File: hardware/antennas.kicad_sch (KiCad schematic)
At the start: 21 parts, among them J1001 132134

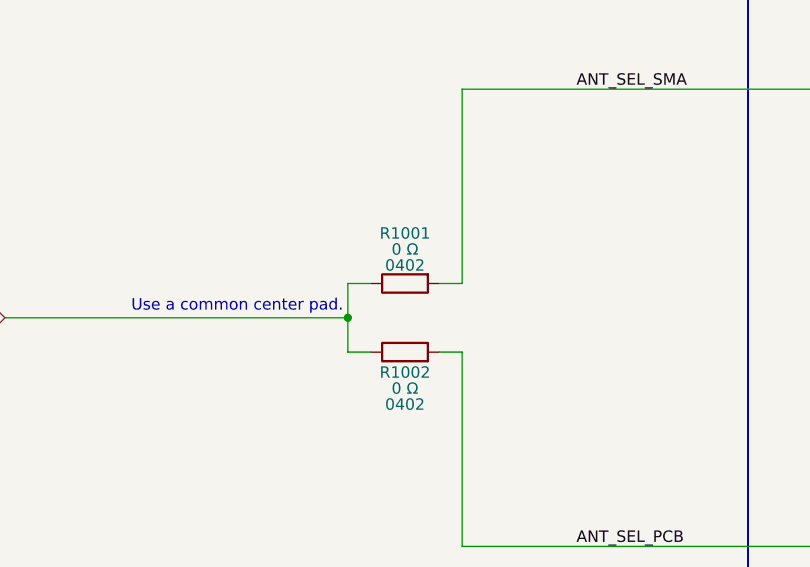
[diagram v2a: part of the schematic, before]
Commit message: HW: Fix BOM and add v5.1.0 to HWID map
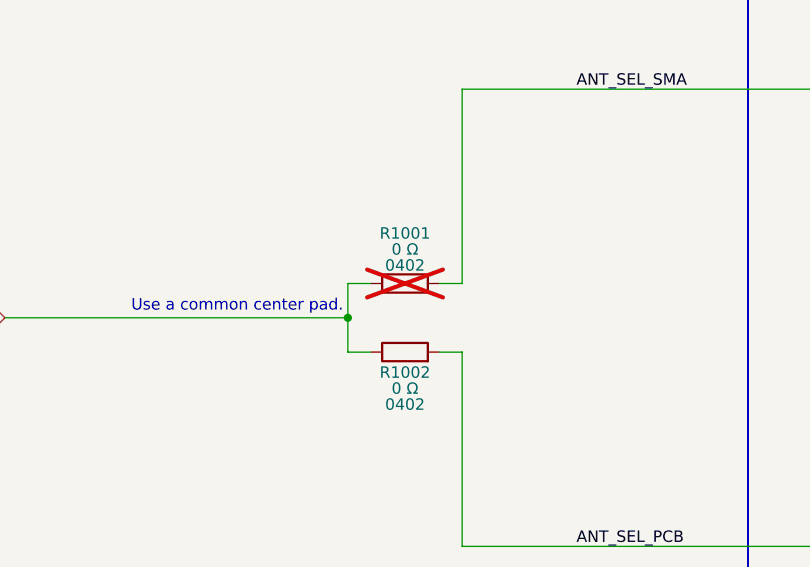
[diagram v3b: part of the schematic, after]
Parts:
- R1001: now not fitted; now left out of the parts list
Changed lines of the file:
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@@
 		(unit 1)
 		(exclude_from_sim no)
-		(in_bom yes)
+		(in_bom no)
 		(on_board yes)
-		(dnp no)
+		(dnp yes)
 		(property "Reference" "R1001"
 			(at 69.85 171.704 90)
